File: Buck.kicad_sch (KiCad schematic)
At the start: 6 parts, among them U1501 XL1509

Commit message: made additions to the project
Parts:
- removed C1501, C1503: 470uF, Capacitor_SMD:CP_Elec_8x10.5, symbol Device:C_Polarized_Small
- removed C1502: 10nF, Resistor_SMD:R_0805_2012Metric_Pad1.20x1.40mm_HandSolder, symbol Device:C_Small
- removed D1501: D_Schottky, Diode_SMD:D_SMA_Handsoldering, symbol Device:D_Schottky
- removed L1501: 47uH, Inductor_SMD:L_6.3x6.3_H3, symbol pspice:INDUCTOR
- removed U1501: XL1509, Package_SO:SOP-8_3.9x4.9mm_P1.27mm, symbol custom_bas:XL1509
- added C1501, C1506: 100nF, Capacitor_SMD:C_0402_1005Metric_Pad0.74x0.62mm_HandSolder, symbol Device:C
- added C1502: 22nF, Capacitor_SMD:C_0402_1005Metric_Pad0.74x0.62mm_HandSolder, symbol Device:C
- added C1503, C1504, C1505: 22uF, Capacitor_SMD:C_0603_1608Metric_Pad1.08x0.95mm_HandSolder, symbol Device:C
- added J1501: power, TerminalBlock_Phoenix:TerminalBlock_Phoenix_MKDS-1,5-2-5.08_1x02_P5.08mm_Horizontal, symbol Connector:Screw_Terminal_01x02
- added L1501: L, Inductor_SMD:L_Bourns-SRU8028_8.0x8.0mm, symbol Device:L
- added R1501: 220k, Resistor_SMD:R_0603_1608Metric_Pad0.98x0.95mm_HandSolder, symbol Device:R
- added R1502: 150k, Resistor_SMD:R_0603_1608Metric_Pad0.98x0.95mm_HandSolder, symbol Device:R
- added R1503: 20k, Resistor_SMD:R_0603_1608Metric_Pad0.98x0.95mm_HandSolder, symbol Device:R
- added U1501: MT2499A, Package_SO:TI_SO-PowerPAD-8, symbol custom_kicad_lib_sk:MT499A
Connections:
- net GND: now also C1503.2, C1504.2, C1505.2, C1506.2, J1501.2 (Pin_2), R1503.2, U1501.4 (GND), U1501.9 (GND)
- net VCC: now also C1503.1, J1501.1 (Pin_1), U1501.2 (Vin), U1501.7 (EN)
- new net: R1501.2, R1502.1, R1503.1, U1501.5 (FB)
- new net: C1501.1, C1502.1, U1501.1 (BS)
- new net: C1501.2, C1502.2, L1501.1, U1501.3 (SW)
- new net +5V: C1504.1, C1505.1, C1506.1, L1501.2, R1501.1, R1502.2

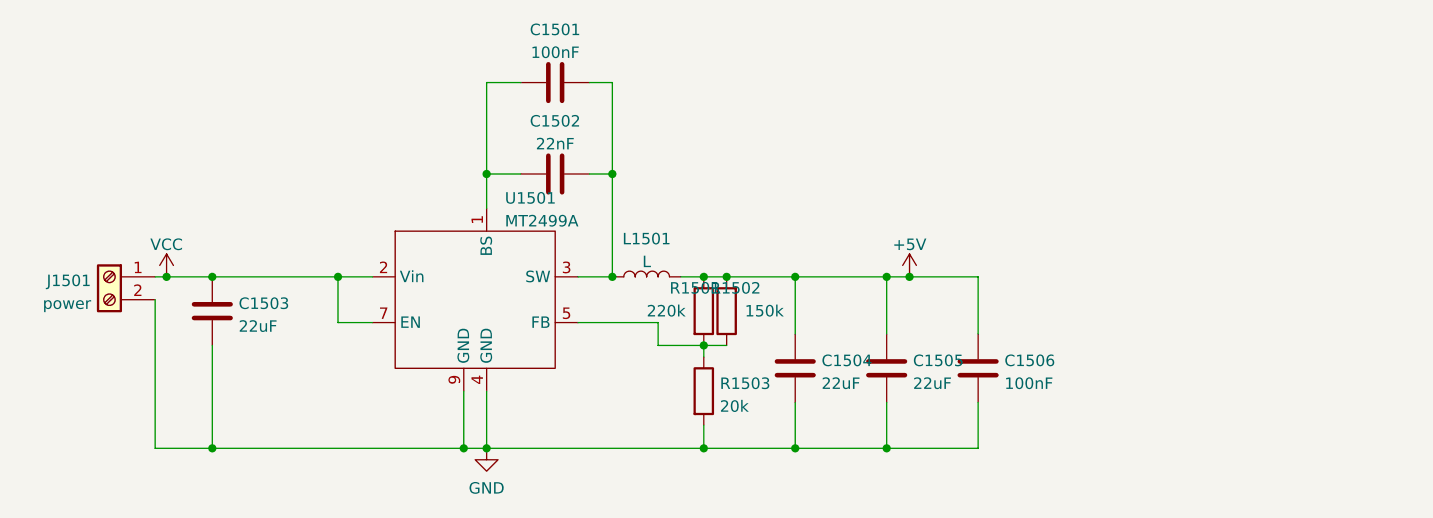
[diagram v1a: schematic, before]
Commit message: added hierarchial labels to some schematics
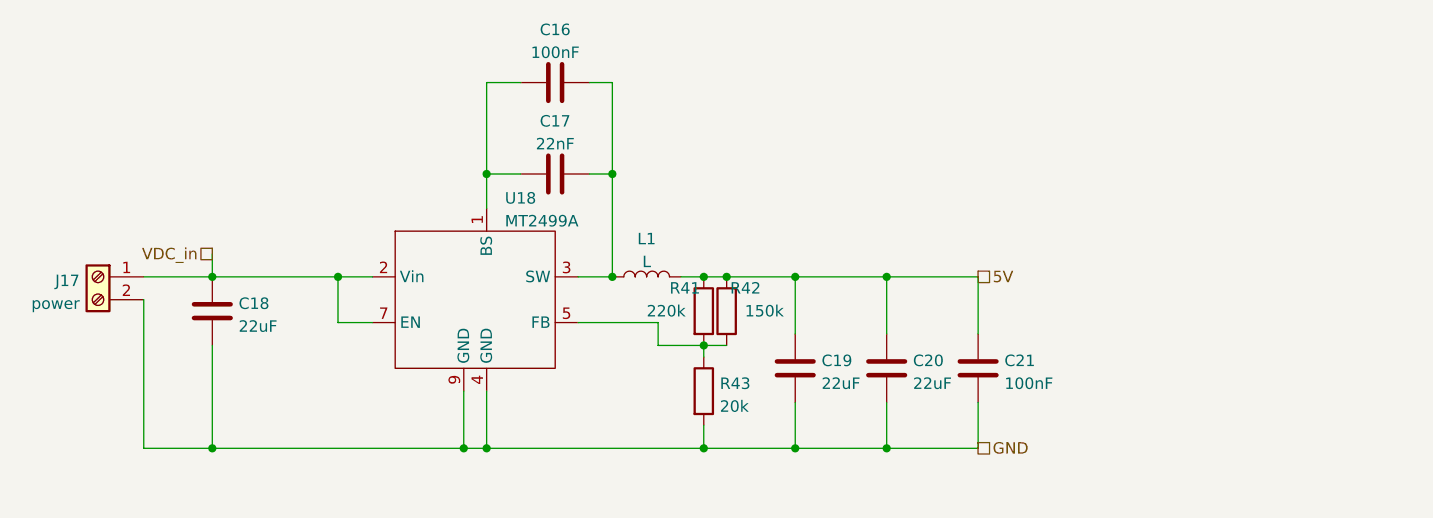
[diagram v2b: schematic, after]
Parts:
- renumbered C1501 to C16, C1502 to C17, C1503 to C18, C1504 to C19, C1505 to C20, C1506 to C21, J1501 to J17, L1501 to L1, R1501 to R41, R1502 to R42, R1503 to R43, U1501 to U18
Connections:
- net +5V renamed 5V
- net VCC renamed VDC_in
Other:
- moved on the sheet: J17
